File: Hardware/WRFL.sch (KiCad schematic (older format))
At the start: 0 parts

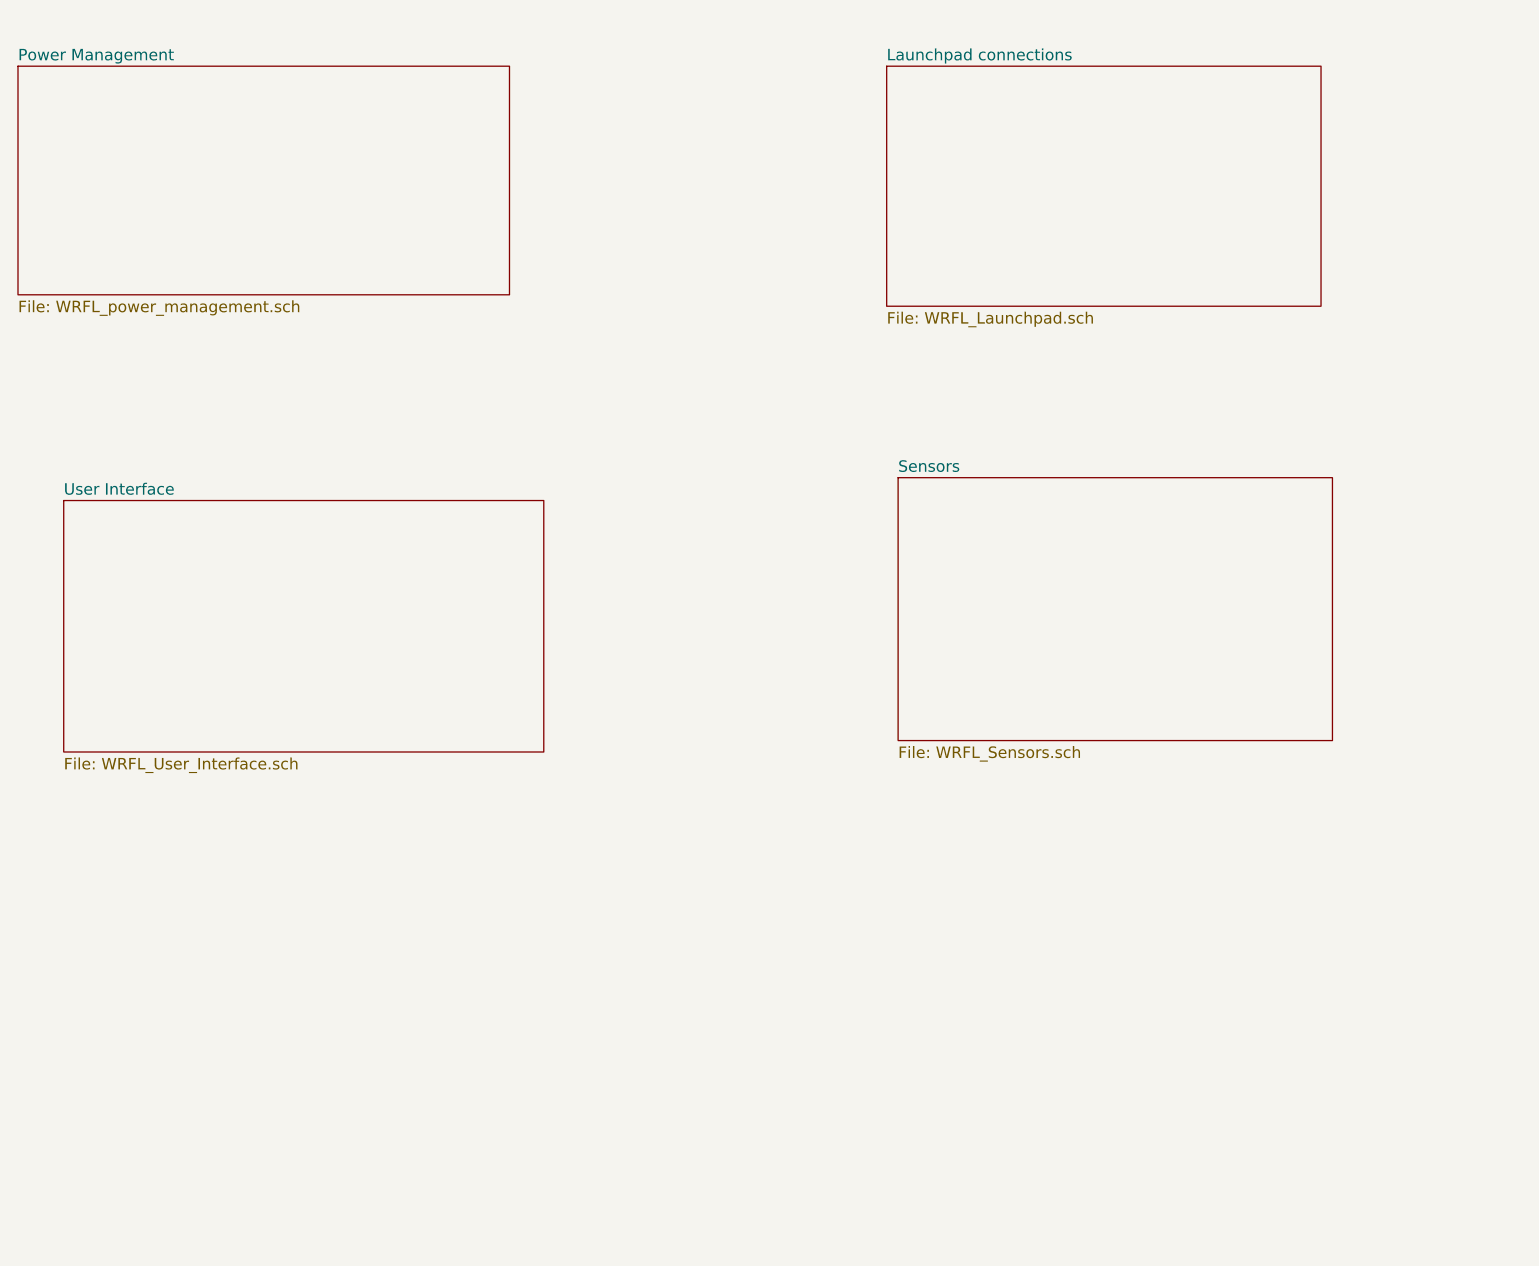
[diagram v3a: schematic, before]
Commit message: Schematics update
Bluetooth sheet added
LCD specific symbol
power management sheet rearrangement
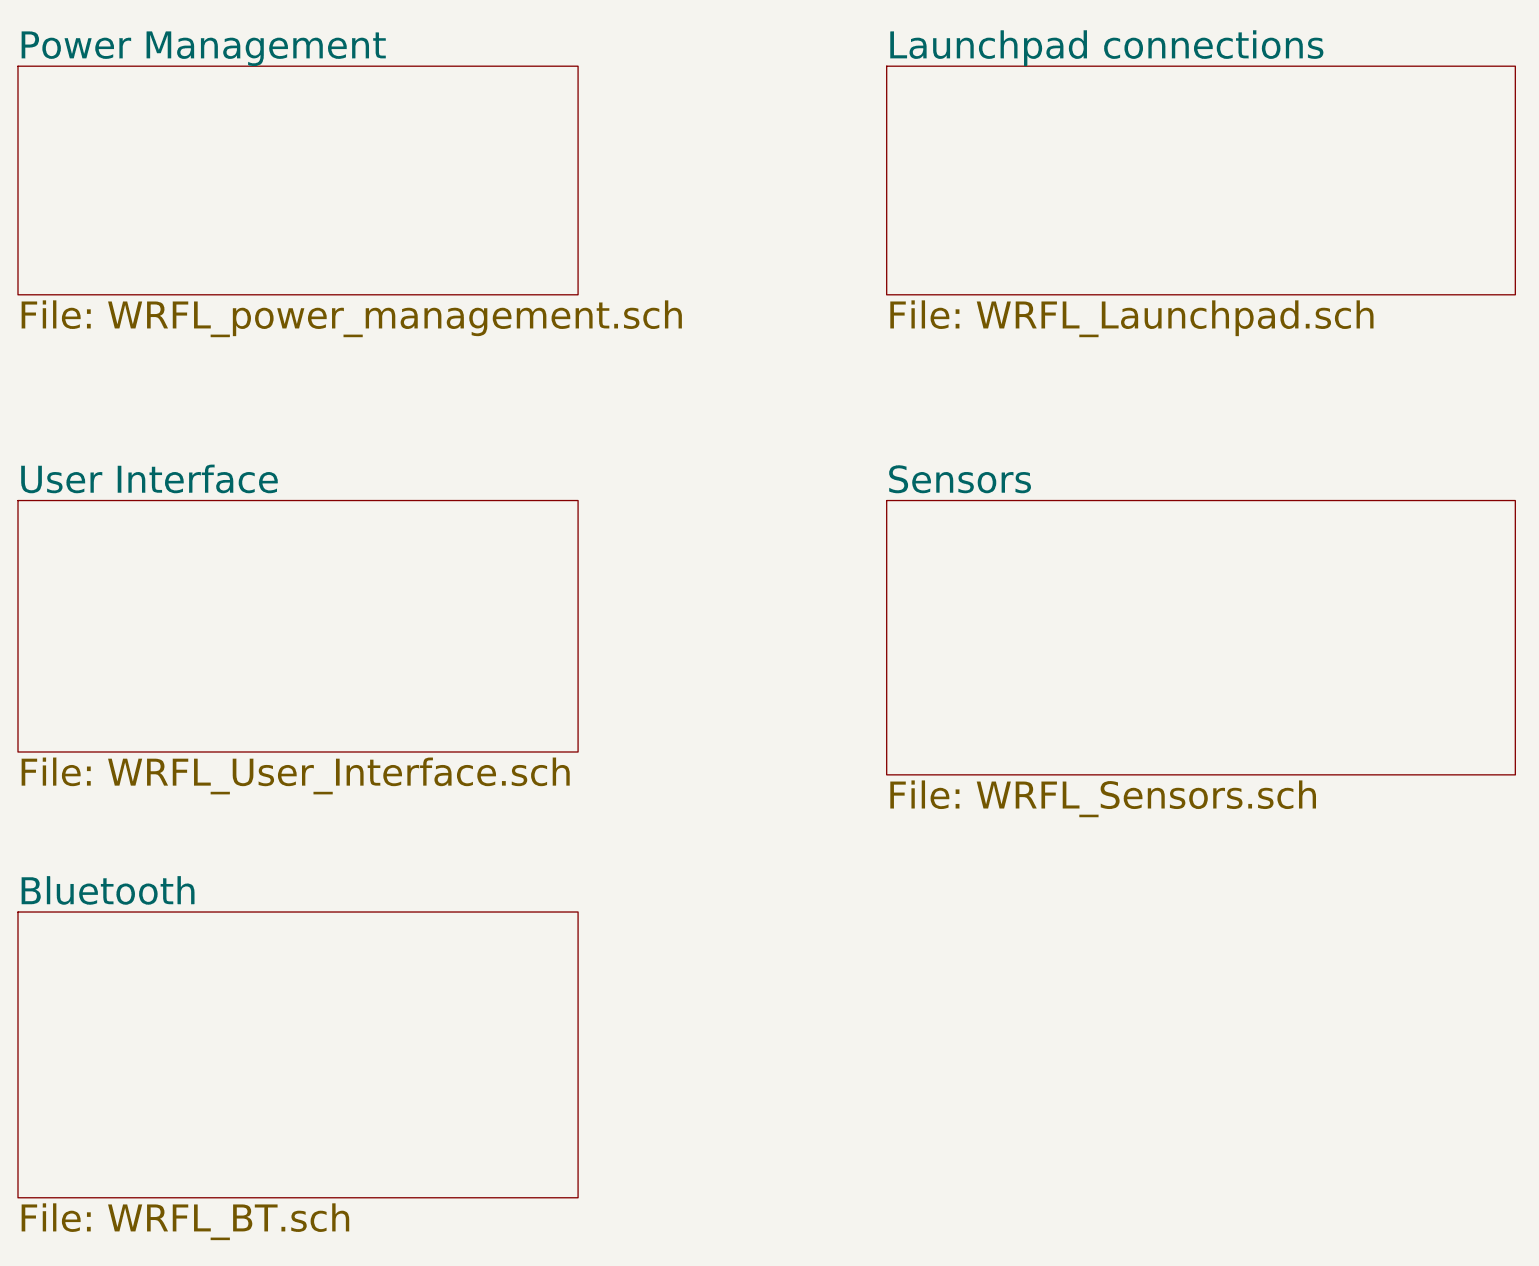
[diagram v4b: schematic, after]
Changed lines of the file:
@@
-EESchema Schematic File Version 2  date Monday, October 07, 2013 12:52:48 PM
+EESchema Schematic File Version 2  date 10/11/2013 1:57:23 AM
 LIBS:power
 LIBS:device
@@
 $Descr A4 11693 8268
 encoding utf-8
-Sheet 1 5
+Sheet 1 6
 Title "WRFL Main"
-Date "7 oct 2013"
+Date "10 oct 2013"
 Rev "1.0"
 Comp "Nightmechanic"
@@
 $EndDescr
 $Sheet
-S 1450 1050 2150 1000
+S 1450 1050 2450 1000
 U 524B45AC
-F0 "Power Management" 50
-F1 "WRFL_power_management.sch" 50
+F0 "Power Management" 118
+F1 "WRFL_power_management.sch" 118
 $EndSheet
 $Sheet
-S 5250 1050 1900 1050
+S 5250 1050 2750 1000
 U 524B4775
-F0 "Launchpad connections" 50
-F1 "WRFL_Launchpad.sch" 50
+F0 "Launchpad connections" 118
+F1 "WRFL_Launchpad.sch" 118
 $EndSheet
 $Sheet
-S 1650 2950 2100 1100
+S 1450 2950 2450 1100
 U 524B49CB
-F0 "User Interface" 50
-F1 "WRFL_User_Interface.sch" 50
+F0 "User Interface" 118
+F1 "WRFL_User_Interface.sch" 118
 $EndSheet
 $Sheet
-S 5300 2850 1900 1150
+S 5250 2950 2750 1200
 U 524B49CD
-F0 "Sensors" 50
-F1 "WRFL_Sensors.sch" 50
+F0 "Sensors" 118
+F1 "WRFL_Sensors.sch" 118
+$EndSheet
+$Sheet
+S 1450 4750 2450 1250
+U 52571324
+F0 "Bluetooth" 118
+F1 "WRFL_BT.sch" 118
 $EndSheet
 $EndSCHEMATC
